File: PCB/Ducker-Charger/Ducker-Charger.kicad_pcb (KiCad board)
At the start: 4 copper layers, 61.8 x 130.1 mm, 194 parts, among them CN1 C_Pack04, IC1 STUSB4710AQ1TR, IC2 TPS54202HDDCT, IC3 BQ34Z100PWR-R2, J1 Conn_01x02, J2 Conn_01x05, J3 Conn_01x02, J4 USB_A, J5 USB_A, J6 Debug, J7 Conn_01x08, J8 Conn_01x07, Q1 BSC040N08NS5, Q10 AO3400A, Q11 AO3400A, Q12 BC846, Q15 BSC040N08NS5, Q16 BSC040N08NS5, Q17 BSC040N08NS5, Q18 BSC040N08NS5, Q19 BSC040N08NS5, Q2 BSC040N08NS5, Q6 AO4407A, Q7 AO3400A, Q8 AO4407A, Q9 AO3400A, SW1 EC11E15244G1, U1 BQ25713RSNR, U2 TPS25750DRJKR, U3 STPD01PUR, U4 TPS54302, U5 INA3221, U6 TPS54302, U7 STM32F401RBT6, U8 BQ7791500PWR, U9 ISO1540DR, Y1 16MHz

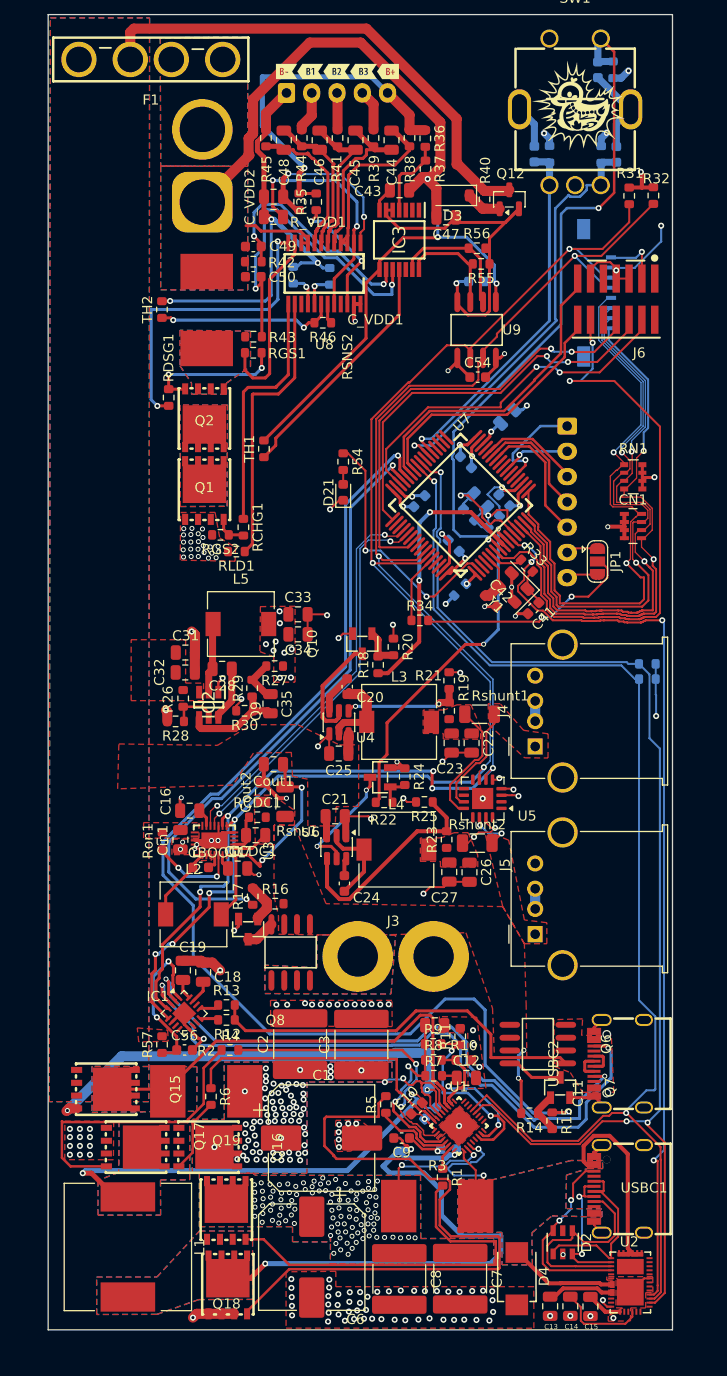
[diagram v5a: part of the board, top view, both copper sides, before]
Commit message: fix: removed 90deg tracks
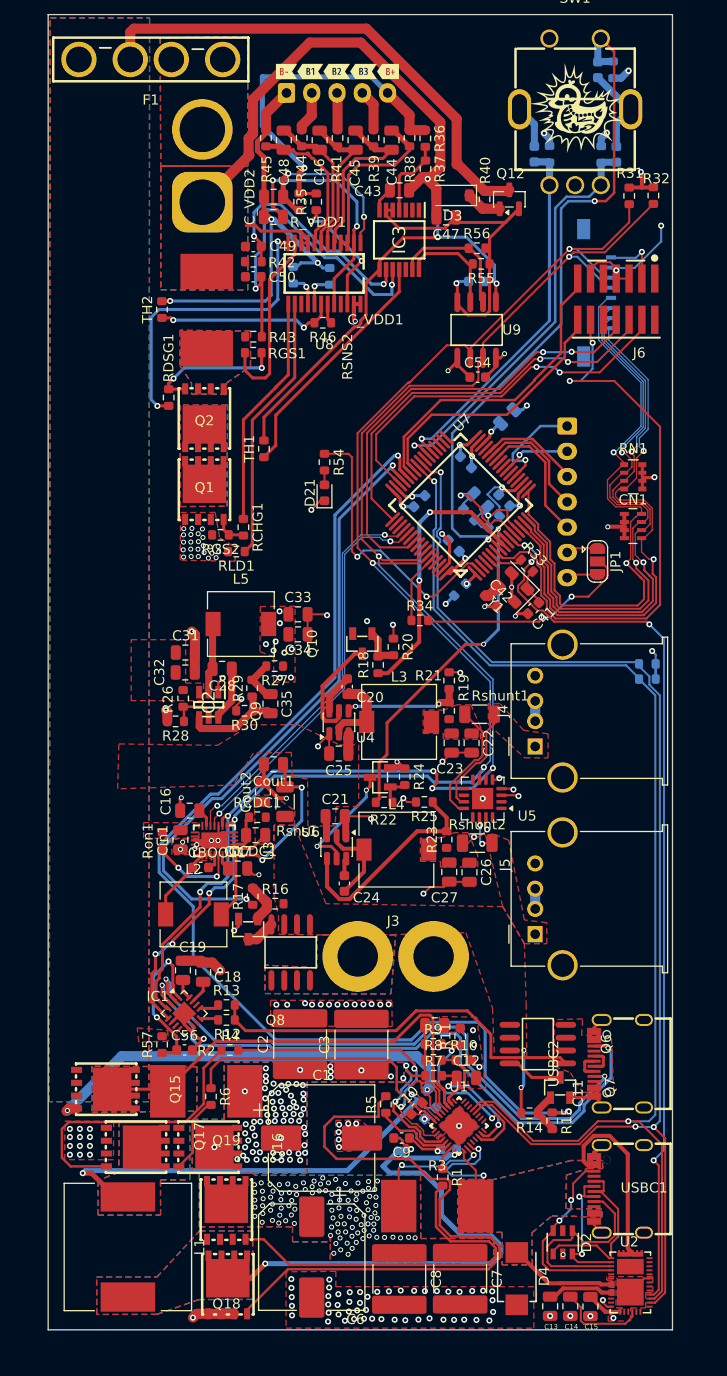
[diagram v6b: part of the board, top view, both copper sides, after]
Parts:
- moved G*** 2.20 mm to (197.8, 82.7)
- moved D21 1.85 mm to (194.7, 63.5)
- moved R54 1.85 mm to (194.7, 60.4)
- moved G*** 0.34 mm to (219.8, 25.3)
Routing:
- net /Logic/MCU_STATUS: track 25.5 -> 28.7 mm
- net /Logic/SWDIO: track 35.9 -> 37.9 mm
- net /High_pow/V_SYS_A: track 13.0 -> 11.2 mm
- net /BMS/I2C_LP.SCL: track 144.1 -> 145.8 mm
- net Net-(U8-CHG): track 24.7 -> 23.1 mm
- net /Logic/LAB_2ENABLER: track 115.0 -> 113.4 mm
- net GND: track 162.0 -> 160.4 mm
- net Net-(Q18-G): track 65.6 -> 64.1 mm
- net Net-(U8-LD): track 28.0 -> 26.5 mm
- net PD_IRQ: track 91.4 -> 90.1 mm
- net /Low_pow/5V_USB_A2: track 5.48 -> 4.25 mm
- net /High_pow/~{BATDRV}: track 46.4 -> 45.1 mm
- net /Logic/NTC_1: track 54.9 -> 56.0 mm
- net /Low_pow/IN-2: track 5.77 -> 4.90 mm
- net Net-(Q19-G): track 39.0 -> 38.1 mm
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
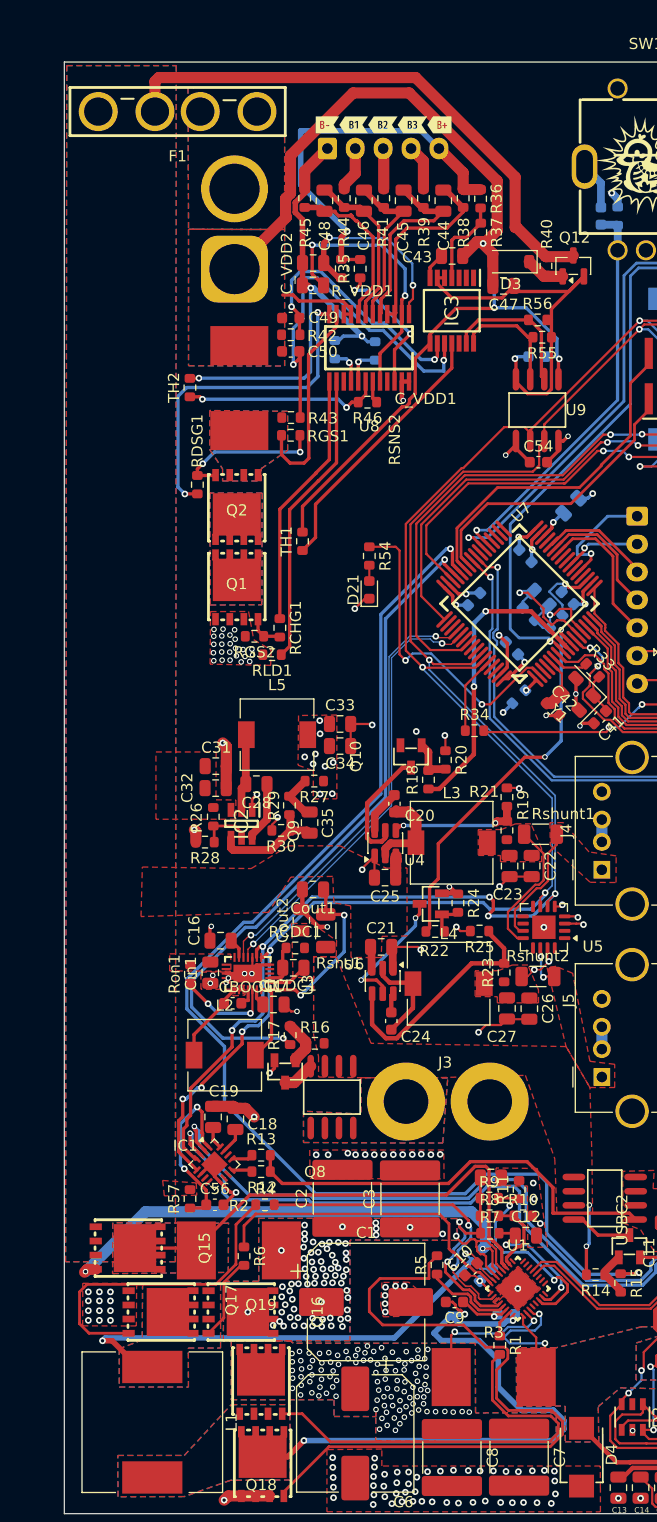
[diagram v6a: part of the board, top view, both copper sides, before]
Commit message: fix: downsized the numbers of load bearing VIAs
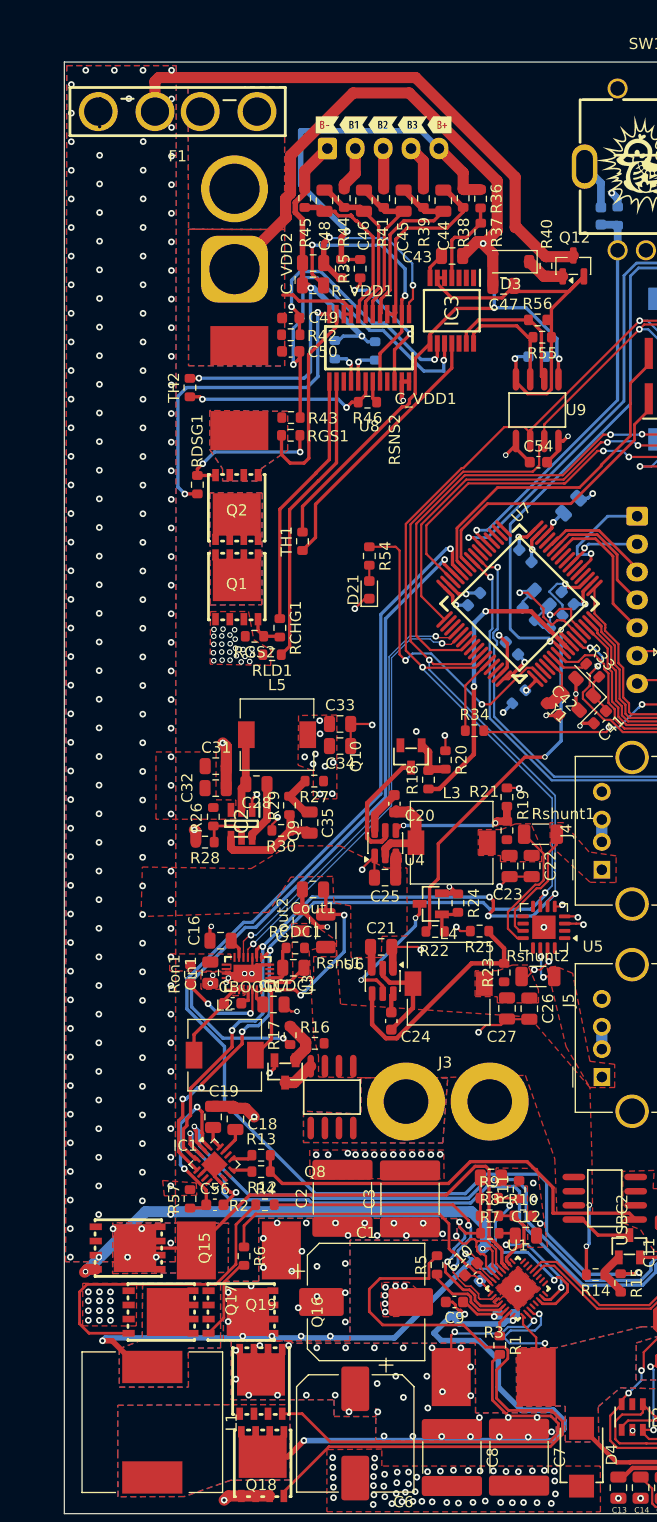
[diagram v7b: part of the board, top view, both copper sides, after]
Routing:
- net /High_pow/V_SYS_A: vias 73 -> 28
- net /High_pow/ACN: vias 108 -> 36
- net +BATT: vias 0 -> 172

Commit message: feat: remade the PCB & minor schematic fixes
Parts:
- removed C1, C6: 220u, Capacitor_SMD:CP_Elec_10x10
- removed C10, C20, C24, C29, C30, C36, C37, C40, C9: 100n, Capacitor_SMD:C_0603_1608Metric
- removed C11, C13, C14, C15: 4.7u, Capacitor_SMD:C_0805_2012Metric
- removed C12, C18, C19, C39: 1u, Capacitor_SMD:C_0805_2012Metric
- removed C16, C17: 4.7u 50V, Capacitor_SMD:C_0805_2012Metric
- removed C2, C3, C7, C8: 22u, Capacitor_SMD:C_2220_5750Metric
- removed C21, C25, C31: 10u, Capacitor_SMD:C_0805_2012Metric
- removed C22, C23, C26, C27, C33, C34: 22u, Capacitor_SMD:C_0805_2012Metric
- removed C28, C32: 0.1u, Capacitor_SMD:C_0805_2012Metric
- removed C35: 75p, Capacitor_SMD:C_0805_2012Metric
- removed C4, C5: 47n, Capacitor_SMD:C_0603_1608Metric
- removed C41, C42: 18p, Capacitor_SMD:C_0603_1608Metric
- removed C56: 1u, Capacitor_SMD:C_0603_1608Metric
- removed CBOOT1: 100n 50V, Capacitor_SMD:C_0603_1608Metric
- removed CCDC1: 4.7n, Capacitor_SMD:C_0805_2012Metric
- removed CN1: C_Pack04, Resistor_SMD:R_Array_Concave_4x0603
- removed CVBAT1: 100n, Resistor_SMD:R_0603_1608Metric
- removed Cin1: 10u 50V, Capacitor_SMD:C_0805_2012Metric
- removed Cout1, Cout2: 22u 25V, Capacitor_SMD:C_0805_2012Metric
- removed D2: USBLC6-4SC6, EasyEDA:SOT-23-6_L2.9-W1.6-P0.95-LS2.8-BL
- removed D21: LED, LED_SMD:LED_0603_1608Metric
- removed D4: SMBJ22A-E3/52, EasyEDA:SMB_L4.3-W3.6-LS5.4-RD
- removed FB1: FerriteBead, Inductor_SMD:L_0603_1608Metric
- removed IC1: STUSB4710AQ1TR, Package_DFN_QFN:QFN-16-1EP_3x3mm_P0.5mm_EP1.7x1.7mm
- removed IC2: TPS54202HDDCT, TPS54202HDDCT:SOT95P280X110-6N
- removed J3: Conn_01x02, TestPoint:TestPoint_Bridge_Pitch6.35mm_Drill1.3mm
- removed J8: Conn_01x07, Connector_JST:JST_XH_S7B-XH-A_1x07_P2.50mm_Horizontal
- removed JP1: Boot, Jumper:SolderJumper-3_P1.3mm_Open_RoundedPad1.0x1.5mm
- removed L1: 2.2u, Inductor_SMD:L_12x12mm_H6mm
- removed L2, L5: 10u, Inductor_SMD:L_6.3x6.3_H3
- removed L3, L4: 10u 5A, Inductor_SMD:L_7.3x7.3_H4.5
- removed Q10, Q11, Q7, Q9: AO3400A, EasyEDA:SOT-23-3_L2.9-W1.3-P1.90-LS2.4-BR
- removed Q15, Q16, Q17, Q18, Q19: BSC040N08NS5, EasyEDA:PG-TDSON-8_L5.9-W5.1-P1.27-LS6.2-BL
- removed Q6, Q8: AO4407A, EasyEDA:SOIC-8_L4.9-W3.9-P1.27-LS6.0-BL
- removed R1, R4, R5, R57, R6, R7: 10, Resistor_SMD:R_0603_1608Metric
- removed R10: 30k, Resistor_SMD:R_0603_1608Metric
- removed R11, R15, R17, R34, R9: 10k, Resistor_SMD:R_0603_1608Metric
- removed R12: 1k2, Resistor_SMD:R_0603_1608Metric
- removed R13: 50, Resistor_SMD:R_0603_1608Metric
- removed R14, R16, R19, R20, R23, R24, R27, Ron1: 100k, Resistor_SMD:R_0603_1608Metric
- removed R18, R22, R33, R54: 1k, Resistor_SMD:R_0603_1608Metric
- removed R2, R3: 5m, EasyEDA:R3920
- removed R21, R25: 13.3k, Resistor_SMD:R_0603_1608Metric
- removed R26: 511k, Resistor_SMD:R_0603_1608Metric
- removed R28: 105k, Resistor_SMD:R_0603_1608Metric
- removed R29: 22.1k, Resistor_SMD:R_0603_1608Metric
- removed R30: 0, Resistor_SMD:R_0603_1608Metric
- removed R8: 20k, Resistor_SMD:R_0603_1608Metric
- removed RCDC1: 5.6k, Resistor_SMD:R_0603_1608Metric
- removed RN1: R_Pack04, Resistor_SMD:R_Array_Convex_4x0603
- removed Rshunt1, Rshunt2, Rsns1: 10m, Resistor_SMD:R_1206_3216Metric
- removed U1: BQ25713RSNR, EasyEDA:QFN-32_L4.0-W4.0-P0.40-TL-EP2.8
- removed U2: TPS25750DRJKR, EasyEDA:QFN-38_L6.0-W4.0-P0.40-TL-EP_RJK
- removed U3: STPD01PUR, EasyEDA:QFN-24_L4.0-W3.0-P0.40-TL-EP
- removed U4, U6: TPS54302, Package_TO_SOT_SMD:SOT-23-6
- removed U5: INA3221, Package_DFN_QFN:Texas_RGV0016A_VQFN-16-1EP_4x4mm_P0.65mm_EP2.1x2.1mm
- removed U7: STM32F401RBT6, EasyEDA:LQFP-64_L10.0-W10.0-P0.50-LS12.0-BL
- removed Y1: 16MHz, Crystal:Crystal_SMD_EuroQuartz_MT-4Pin_3.2x2.5mm
- added C201: 1u, Capacitor_SMD:C_0805_2012Metric, B.Cu at (95.9, 172.6)
- added C202: 1u, Capacitor_SMD:C_0805_2012Metric, F.Cu at (124.6, 169.9)
- added C203: 10u 35V, Capacitor_SMD:C_1206_3216Metric, F.Cu at (123.4, 166.5)
- added C204: 10u 35V, Capacitor_SMD:C_1206_3216Metric, F.Cu at (121.1, 166.5)
- added C205: 3.3u, Capacitor_SMD:C_0805_2012Metric, F.Cu at (88.9, 173.0)
- added C206: 10u 35V, Capacitor_SMD:C_1206_3216Metric, F.Cu at (118.8, 166.5)
- added C207: 10u 16V, Capacitor_SMD:C_0603_1608Metric, F.Cu at (120.9, 150.7)
- added C208: 10u 35V, Capacitor_SMD:C_1206_3216Metric, F.Cu at (116.5, 166.5)
- added C209: 10u 35V, Capacitor_SMD:C_1206_3216Metric, F.Cu at (114.2, 166.5)
- added C210: 10u 35V, Capacitor_SMD:C_1206_3216Metric, F.Cu at (111.9, 166.5)
- added C211: 470n, Capacitor_SMD:C_0805_2012Metric, F.Cu at (110.9, 169.8)
- added C212: 10u 35V, Capacitor_SMD:C_1206_3216Metric, F.Cu at (117.1, 159.8)
- added C213: 22u 35V, Capacitor_SMD:C_1210_3225Metric, B.Cu at (117.1, 159.8)
- added C214: 33p, Capacitor_SMD:C_0603_1608Metric, F.Cu at (93.9, 161.5)
- added C215: 33n, Capacitor_SMD:C_0603_1608Metric, F.Cu at (99.9, 167.3)
- added C216: 22u 35V, Capacitor_SMD:C_1210_3225Metric, B.Cu at (117.1, 156.6)
- added C217: 1800p, Capacitor_SMD:C_0603_1608Metric, F.Cu at (92.4, 159.5)
- added C218: 680p, Capacitor_SMD:C_0603_1608Metric, F.Cu at (89.4, 159.0)
- added C219: 4.7u, Capacitor_SMD:C_0805_2012Metric, B.Cu at (131.6, 153.8)
- added C220: 100u 16V, Capacitor_SMD:C_1210_3225Metric, F.Cu at (116.9, 149.7)
- added C221: 15p, Capacitor_SMD:C_0603_1608Metric, F.Cu at (90.9, 161.0)
- added C222: 10n, Capacitor_SMD:C_0603_1608Metric, F.Cu at (106.5, 174.9)
- added C223: 100u 16V, Capacitor_SMD:C_1210_3225Metric, F.Cu at (113.6, 149.7)
- added C224: 100p, Capacitor_SMD:C_0603_1608Metric, B.Cu at (97.5, 165.0)
- added C225: 100u 16V, Capacitor_SMD:C_1210_3225Metric, F.Cu at (110.4, 149.7)
- added C226: 10u 16V, Capacitor_SMD:C_0603_1608Metric, F.Cu at (119.4, 150.7)
- added C227: 100p, Capacitor_SMD:C_0603_1608Metric, B.Cu at (93.8, 162.3)
- added C228: 10u, Capacitor_SMD:C_0805_2012Metric, F.Cu at (105.9, 155.7)
- added C229: 47n, Capacitor_SMD:C_0603_1608Metric, F.Cu at (92.7, 172.5)
- added C230: 10u, Capacitor_SMD:C_0805_2012Metric, F.Cu at (105.8, 153.7)
- added C231: 47n, Capacitor_SMD:C_0603_1608Metric, F.Cu at (74.9, 177.6)
- added C232: 10u 25V, Capacitor_SMD:C_1206_3216Metric, F.Cu at (92.9, 87.9)
- added C233: 330p, Capacitor_SMD:C_0603_1608Metric, B.Cu at (115.1, 149.9)
- added C234: 330p, Capacitor_SMD:C_0603_1608Metric, B.Cu at (115.2, 148.4)
- added C235: 10u 25V, Capacitor_SMD:C_1206_3216Metric, F.Cu at (73.4, 166.3)
- added C236: 10u 25V, Capacitor_SMD:C_1206_3216Metric, F.Cu at (73.4, 164.0)
- added C237: 10u 25V, Capacitor_SMD:C_1206_3216Metric, F.Cu at (73.4, 175.7)
- added C238: 10u 25V, Capacitor_SMD:C_1206_3216Metric, F.Cu at (73.4, 173.3)
- added C239: 10u 25V, Capacitor_SMD:C_1206_3216Metric, F.Cu at (73.4, 171.0)
- added C240: 10u 25V, Capacitor_SMD:C_1206_3216Metric, F.Cu at (73.4, 168.7)
- added C241: 1u, Capacitor_SMD:C_0805_2012Metric, F.Cu at (82.3, 159.5)
- added C242: 100n, Capacitor_SMD:C_0603_1608Metric, F.Cu at (99.9, 84.9)
- added C243: 0.1, Capacitor_SMD:C_0805_2012Metric, F.Cu at (74.7, 152.4)
- added C244: 22u 16V, Capacitor_SMD:C_0805_2012Metric, F.Cu at (94.9, 81.4)
- added C245: 22u 16V, Capacitor_SMD:C_0805_2012Metric, F.Cu at (92.4, 81.4)
- added C246: 100n, Capacitor_SMD:C_0603_1608Metric, F.Cu at (108.0, 150.5)
- added C301: 4.7u 50V, Capacitor_SMD:C_0805_2012Metric, F.Cu at (86.3, 137.7)
- added C302: 4.7u 50V, Capacitor_SMD:C_0805_2012Metric, B.Cu at (96.8, 135.4)
- added C303: 10u 25V, Capacitor_SMD:C_1206_3216Metric, F.Cu at (93.0, 100.6)
- added C304: 10u 25V, Capacitor_SMD:C_1206_3216Metric, F.Cu at (93.0, 122.8)
- added C305: 1u, Capacitor_SMD:C_0805_2012Metric, F.Cu at (118.3, 139.0)
- added C306: 100n, Capacitor_SMD:C_0603_1608Metric, F.Cu at (100.0, 97.6)
- added C307: 100n, Capacitor_SMD:C_0603_1608Metric, F.Cu at (100.0, 119.8)
- added C308: 1u, Capacitor_SMD:C_0603_1608Metric, F.Cu at (122.9, 138.0)
- added C309: 1u, Capacitor_SMD:C_0805_2012Metric, F.Cu at (120.3, 139.0)
- added C310: 22u, Capacitor_SMD:C_0805_2012Metric, F.Cu at (92.5, 94.1)
- added C311: 22u, Capacitor_SMD:C_0805_2012Metric, F.Cu at (95.0, 116.3)
- added C312: 22u, Capacitor_SMD:C_0805_2012Metric, F.Cu at (95.0, 94.1)
- added C313: 22u, Capacitor_SMD:C_0805_2012Metric, F.Cu at (92.5, 116.3)
- added C401: 100n, Capacitor_SMD:C_0603_1608Metric, B.Cu at (119.6, 64.2)
- added C402: 100n, Capacitor_SMD:C_0603_1608Metric, B.Cu at (117.9, 76.4)
- added C404: 1u, Capacitor_SMD:C_0805_2012Metric, F.Cu at (130.6, 78.7)
- added C405: 100n, Capacitor_SMD:C_0603_1608Metric, F.Cu at (128.6, 78.7)
- added C406: 100n, Capacitor_SMD:C_0603_1608Metric, B.Cu at (124.6, 68.4)
- added C407: 100n, Capacitor_SMD:C_0603_1608Metric, B.Cu at (106.9, 68.9)
- added C409: 18p, Capacitor_SMD:C_0603_1608Metric, F.Cu at (126.1, 82.4)
- added C412: 18p, Capacitor_SMD:C_0603_1608Metric, F.Cu at (121.1, 81.2)
- added C413: 10u 25V, Capacitor_SMD:C_1206_3216Metric, F.Cu at (92.7, 111.7)
- added C414: 0.1u, Capacitor_SMD:C_0805_2012Metric, F.Cu at (95.2, 111.7)
- added C415: 100n, Capacitor_SMD:C_0603_1608Metric, B.Cu at (130.1, 45.6)
- added C416: 100n, Capacitor_SMD:C_0805_2012Metric, F.Cu at (100.2, 108.7)
- added C417: 22u, Capacitor_SMD:C_0805_2012Metric, F.Cu at (95.2, 105.3)
- added C418: 22u, Capacitor_SMD:C_0805_2012Metric, F.Cu at (92.7, 105.3)
- added C419: 75p, Capacitor_SMD:C_0805_2012Metric, F.Cu at (107.7, 111.7)
- added C420: 100n, Capacitor_SMD:C_0603_1608Metric, F.Cu at (129.2, 65.2)
- added CBOOT301: 100n 50V, Capacitor_SMD:C_0603_1608Metric, F.Cu at (96.8, 136.5)
- added CCDC301: 4.7n, Capacitor_SMD:C_0805_2012Metric, F.Cu at (93.6, 131.1)
- added CN401: 100n, Resistor_SMD:R_Array_Concave_4x0603, F.Cu at (130.2, 69.5)
- added CVBAT401: 100n, Resistor_SMD:R_0603_1608Metric, B.Cu at (111.9, 81.9)
- added Cin301: 10u 50V, Capacitor_SMD:C_0805_2012Metric, F.Cu at (87.0, 141.7)
- added Cout301: 22u 35V, Capacitor_SMD:C_1210_3225Metric, F.Cu at (105.7, 142.0)
- added Cout302: 22u 35V, Capacitor_SMD:C_1210_3225Metric, F.Cu at (111.0, 142.1)
- added D201: USBLC6-4SC6, EasyEDA:SOT-23-6_L2.9-W1.6-P0.95-LS2.8-BL, B.Cu at (123.2, 155.5)
- added D202: LED, LED_SMD:LED_0603_1608Metric, F.Cu at (106.0, 159.7)
- added D301: USBLC6-4SC6, EasyEDA:SOT-23-6_L2.9-W1.6-P0.95-LS2.8-BL, B.Cu at (123.3, 135.7)
- added D401: LED, LED_SMD:LED_0603_1608Metric, F.Cu at (120.2, 85.2)
- added FB401: FerriteBead, Inductor_SMD:L_0603_1608Metric, F.Cu at (126.9, 78.7)
- added G***: LOGO, LOGO, F.Cu at (176.7, 110.9)
- added IC301: STUSB4710AQ1TR, Package_DFN_QFN:QFN-16-1EP_3x3mm_P0.5mm_EP1.7x1.7mm, F.Cu at (118.8, 135.1)
- added IC401: TPS54202HDDCT, TPS54202HDDCT:SOT95P280X110-6N, F.Cu at (98.5, 111.7)
- added J303: Conn_01x02, TerminalBlock:TerminalBlock_bornier-2_P5.08mm, B.Cu at (125.1, 125.8)
- added J404: Conn_01x08, Connector_JST:JST_EH_B8B-EH-A_1x08_P2.50mm_Vertical, F.Cu at (97.4, 67.2)
- added JP401: Boot, Jumper:SolderJumper-3_P1.3mm_Open_RoundedPad1.0x1.5mm, F.Cu at (107.1, 81.2)
- added JP402: BL_NODE, Jumper:SolderJumper-3_P1.3mm_Open_RoundedPad1.0x1.5mm, B.Cu at (119.6, 55.4)
- added L201: 2.2u 20A, Inductor_SMD:L_Chilisin_BMRF00131360, F.Cu at (90.6, 180.8)
- added L202: 10u 5A, Inductor_SMD:L_7.3x7.3_H4.5, F.Cu at (87.4, 85.4)
- added L301: 10u 5A, Inductor_SMD:L_7.3x7.3_H4.5, F.Cu at (98.5, 141.2)
- added L302: 10u 5A, Inductor_SMD:L_7.3x7.3_H4.5, F.Cu at (87.5, 98.1)
- added L303: 10u 5A, Inductor_SMD:L_7.3x7.3_H4.5, F.Cu at (87.5, 120.3)
- added L401: 10u, Inductor_SMD:L_6.3x6.3_H3, F.Cu at (87.7, 109.2)
- added NT401: NetTie_2, NetTie:NetTie-2_SMD_Pad0.5mm, F.Cu at (128.6, 80.2)
- added Q201: BSC040N08NS5, EasyEDA:PG-TDSON-8_L5.9-W5.1-P1.27-LS6.2-BL, F.Cu at (100.1, 173.9)
- added Q202: BSC040N08NS5, EasyEDA:PG-TDSON-8_L5.9-W5.1-P1.27-LS6.2-BL, F.Cu at (101.9, 180.9)
- added Q203: BSC040N08NS5, EasyEDA:PG-TDSON-8_L5.9-W5.1-P1.27-LS6.2-BL, F.Cu at (78.1, 180.8)
- added Q204: BSC040N08NS5, EasyEDA:PG-TDSON-8_L5.9-W5.1-P1.27-LS6.2-BL, F.Cu at (79.3, 174.4)
- added Q205: AO4407A, EasyEDA:SOIC-8_L4.9-W3.9-P1.27-LS6.0-BL, F.Cu at (79.4, 164.4)
- added Q301: AO3400A, EasyEDA:SOT-23-3_L2.9-W1.3-P1.90-LS2.4-BR, B.Cu at (103.5, 98.0)
- added Q302: AO3400A, EasyEDA:SOT-23-3_L2.9-W1.3-P1.90-LS2.4-BR, B.Cu at (103.5, 120.2)
- added Q303: AO3400A, EasyEDA:SOT-23-3_L2.9-W1.3-P1.90-LS2.4-BR, B.Cu at (105.6, 138.3)
- added Q304: AO3400A, EasyEDA:SOT-23-3_L2.9-W1.3-P1.90-LS2.4-BR, B.Cu at (105.7, 130.8)
- added Q305: AO4407A, EasyEDA:SOIC-8_L4.9-W3.9-P1.27-LS6.0-BL, B.Cu at (111.6, 140.2)
- added Q306: AO4407A, EasyEDA:SOIC-8_L4.9-W3.9-P1.27-LS6.0-BL, B.Cu at (111.7, 132.7)
- added Q401: AO3400A, EasyEDA:SOT-23-3_L2.9-W1.3-P1.90-LS2.4-BR, B.Cu at (113.6, 54.0)
- added Q402: PMOS, EasyEDA:SOT-23-3_L2.9-W1.3-P1.90-LS2.4-BR, B.Cu at (113.9, 57.6)
- added R201: 10, Resistor_SMD:R_0603_1608Metric, B.Cu at (95.8, 170.9)
- added R202: 10k, Resistor_SMD:R_0603_1608Metric, B.Cu at (111.6, 159.6)
- added R203: 383k, Resistor_SMD:R_0603_1608Metric, F.Cu at (97.4, 166.5)
- added R204: 220k, Resistor_SMD:R_0603_1608Metric, F.Cu at (97.4, 168.0)
- added R205: 2.2, Resistor_SMD:R_0603_1608Metric, F.Cu at (125.3, 165.7)
- added R206: 10k, Resistor_SMD:R_0603_1608Metric, B.Cu at (111.6, 161.1)
- added R207: 330k, Resistor_SMD:R_0603_1608Metric, F.Cu at (87.9, 162.5)
- added R208: 1M, Resistor_SMD:R_0603_1608Metric, F.Cu at (86.4, 162.0)
- added R209: 1, Resistor_SMD:R_0603_1608Metric, F.Cu at (110.0, 165.7)
- added R210: 4.99, Resistor_SMD:R_0603_1608Metric, F.Cu at (102.2, 166.5)
- added R211: 40.2k, Resistor_SMD:R_0603_1608Metric, F.Cu at (92.4, 162.5)
- added R212: 10m, EasyEDA:R3920, F.Cu at (106.5, 167.3)
- added R213: 10k, Resistor_SMD:R_0603_1608Metric, F.Cu at (89.4, 162.5)
- added R214: 4.99, Resistor_SMD:R_0603_1608Metric, F.Cu at (102.2, 168.0)
- added R215: 137k, Resistor_SMD:R_0603_1608Metric, B.Cu at (97.5, 163.5)
- added R216: 10k, Resistor_SMD:R_0603_1608Metric, B.Cu at (96.3, 169.4)
- added R217: 30k, Resistor_SMD:R_0603_1608Metric, B.Cu at (92.1, 161.6)
- added R218: 150k, Resistor_SMD:R_0603_1608Metric, B.Cu at (100.9, 85.3)
- added R219: 27k, Resistor_SMD:R_0603_1608Metric, B.Cu at (100.9, 88.7)
- added R220: 10, Resistor_SMD:R_0603_1608Metric, F.Cu at (71.9, 153.6)
- added R221: 10m, EasyEDA:R3920, F.Cu at (79.5, 152.6)
- added R222: 10, Resistor_SMD:R_0603_1608Metric, F.Cu at (71.9, 151.1)
- added R223: 1k, Resistor_SMD:R_0603_1608Metric, F.Cu at (106.1, 157.7)
- added R224: 100k, Resistor_SMD:R_0603_1608Metric, F.Cu at (104.5, 87.9)
- added R225: 13.3k, Resistor_SMD:R_0603_1608Metric, F.Cu at (102.4, 87.9)
- added R301: 1k, Resistor_SMD:R_0603_1608Metric, B.Cu at (103.0, 94.5)
- added R302: 1k, Resistor_SMD:R_0603_1608Metric, B.Cu at (103.0, 116.7)
- added R303: 100k, Resistor_SMD:R_0603_1608Metric, B.Cu at (105.5, 95.5)
- added R304: 100k, Resistor_SMD:R_0603_1608Metric, B.Cu at (105.5, 117.7)
- added R305: 10k, Resistor_SMD:R_0603_1608Metric, B.Cu at (104.2, 142.7)
- added R306: 10k, Resistor_SMD:R_0603_1608Metric, B.Cu at (104.3, 134.9)
- added R307: 100k, Resistor_SMD:R_0603_1608Metric, B.Cu at (106.6, 141.9)
- added R308: 100k, Resistor_SMD:R_0603_1608Metric, B.Cu at (106.7, 134.4)
- added R309: 10k, Resistor_SMD:R_0603_1608Metric, B.Cu at (101.0, 98.1)
- added R310: 10k, Resistor_SMD:R_0603_1608Metric, B.Cu at (101.0, 120.3)
- added R311: 10, Resistor_SMD:R_0603_1608Metric, F.Cu at (122.1, 140.3)
- added R312: 100k, Resistor_SMD:R_0603_1608Metric, F.Cu at (104.5, 100.6)
- added R313: 13.3k, Resistor_SMD:R_0603_1608Metric, F.Cu at (102.5, 100.6)
- added R314: 100k, Resistor_SMD:R_0603_1608Metric, F.Cu at (104.5, 122.8)
- added R315: 13.3k, Resistor_SMD:R_0603_1608Metric, F.Cu at (102.5, 122.8)
- added R316: 1k2, Resistor_SMD:R_0603_1608Metric, F.Cu at (123.8, 133.8)
- added R317: 50, Resistor_SMD:R_0603_1608Metric, F.Cu at (125.0, 139.5)
- added R402: 220, Resistor_SMD:R_0603_1608Metric, F.Cu at (123.6, 78.9)
- added R405: 511k, Resistor_SMD:R_0603_1608Metric, B.Cu at (102.4, 112.0)
- added R406: 105k, Resistor_SMD:R_0603_1608Metric, B.Cu at (100.2, 112.0)
- added R407: 10k, Resistor_SMD:R_0603_1608Metric, F.Cu at (109.9, 80.2)
- added R408: 1k, Resistor_SMD:R_0603_1608Metric, F.Cu at (119.1, 82.3)
- added R413: 22.1k, Resistor_SMD:R_0603_1608Metric, F.Cu at (105.7, 111.7)
- added R414: 4k87, Resistor_SMD:R_0603_1608Metric, F.Cu at (103.7, 111.7)
- added R415: 10k, Resistor_SMD:R_0603_1608Metric, F.Cu at (127.6, 66.9)
- added R416: 1k, Resistor_SMD:R_0603_1608Metric, B.Cu at (117.6, 54.1)
- added R417: 10k, Resistor_SMD:R_0603_1608Metric, B.Cu at (116.1, 54.1)
- added R418: 1k, Resistor_SMD:R_0603_1608Metric, B.Cu at (117.6, 57.1)
- added R419: 10k, Resistor_SMD:R_0603_1608Metric, B.Cu at (116.1, 57.1)
- added R420: 4k7, Resistor_SMD:R_0603_1608Metric, B.Cu at (114.6, 65.8)
- added RCDC301: 10k, Resistor_SMD:R_0603_1608Metric, F.Cu at (91.1, 132.1)
- added RCDC302: 5.6k, Resistor_SMD:R_0603_1608Metric, F.Cu at (93.4, 132.9)
- added RN401: 10k, Resistor_SMD:R_Array_Convex_4x0603, F.Cu at (130.4, 74.4)
- added Ron301: 100k, Resistor_SMD:R_0603_1608Metric, B.Cu at (96.6, 137.2)
- added Rshunt301: 10m, Resistor_SMD:R_1206_3216Metric, F.Cu at (113.6, 94.9)
- added Rshunt302: 10m, Resistor_SMD:R_1206_3216Metric, F.Cu at (113.7, 112.9)
- added Rsns301: 25m, Resistor_SMD:R_1206_3216Metric, F.Cu at (108.1, 138.3)
- added SW403: Reset, Button_Switch_SMD:SW_SPST_FSMSM, B.Cu at (132.9, 43.0)
- added TH401: Thermistor_NTC, Resistor_SMD:R_0603_1608Metric, F.Cu at (126.4, 64.2)
- added U201: BQ25713RSNR, EasyEDA:QFN-32_L4.0-W4.0-P0.40-TL-EP2.8, F.Cu at (90.9, 167.5)
- added U202: TPS25750DRJKR, EasyEDA:QFN-38_L6.0-W4.0-P0.40-TL-EP_RJK, F.Cu at (111.2, 155.0)
- added U203: TPS54302, Package_TO_SOT_SMD:SOT-23-6, F.Cu at (98.1, 87.9)
- added U301: INA3221, Package_DFN_QFN:Texas_RGV0016A_VQFN-16-1EP_4x4mm_P0.65mm_EP2.1x2.1mm, B.Cu at (113.2, 103.9)
- added U302: STPD01PUR, EasyEDA:QFN-24_L4.0-W3.0-P0.40-TL-EP, F.Cu at (91.2, 136.9)
- added U303: TPS54302, Package_TO_SOT_SMD:SOT-23-6, F.Cu at (98.3, 100.6)
- added U304: TPS54302, Package_TO_SOT_SMD:SOT-23-6, F.Cu at (98.3, 122.8)
- added U401: STM32F401RBT6, EasyEDA:LQFP-64_L10.0-W10.0-P0.50-LS12.0-BL, F.Cu at (115.9, 72.9)
- added Y401: 16MHz, Crystal:Crystal_SMD_EuroQuartz_MT-4Pin_3.2x2.5mm, F.Cu at (123.6, 81.9)
- D501: renamed from D3; value D_Zener -> 5V
- R515: renamed from R40; value 220k -> 15k
- RDSG501: renamed from RDSG1; value 4k5 -> 1k
- moved R410 122.4 mm to (131.0, 156.7), turned to -90 degrees
- moved R412 120.3 mm to (132.5, 156.7), turned to -90 degrees
- moved R411 106.0 mm to (120.2, 51.4)
- moved R409 106.0 mm to (122.6, 51.3)
- moved USBC201 96.7 mm to (130.1, 155.9)
- moved USBC301 95.3 mm to (130.0, 136.2)
- moved TH502 94.9 mm to (94.6, 71.2)
- moved J301 94.3 mm to (121.7, 97.8)
- moved C403 94.3 mm to (127.9, 30.5)
- moved C410 94.3 mm to (121.6, 38.9)
- moved C501 94.3 mm to (107.5, 37.5)
- moved C502 94.3 mm to (103.9, 37.5)
- moved C504 94.3 mm to (96.8, 37.5)
- moved F101 94.3 mm to (83.7, 29.5)
- moved IC501 94.3 mm to (108.2, 47.3)
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- renumbered C53 to C403, C38 to C408, C51 to C410, C52 to C411, C44 to C501, C45 to C502, C46 to C503, C48 to C504, C49 to C505, C50 to C506, C55 to C507, C54 to C508, C43 to C509, C47 to C510, C_VDD1 to C_VDD501, C_VDD2 to C_VDD502, F1 to F101, IC3 to IC501, J1 to J101, J2 to J102, J4 to J301, J5 to J302, J6 to J401, J7 to J403, Q1 to Q501, Q2 to Q502, Q12 to Q503, R51 to R401, R49 to R403, R50 to R404, R32 to R409, R53 to R410, R31 to R411, R52 to R412, R47 to R501, R38 to R502, R39 to R503, R41 to R504, R44 to R505, R45 to R506, R48 to R507, R42 to R508, R43 to R509, R46 to R510, R35 to R511, R36 to R512, R37 to R513, R56 to R514, R55 to R516, RCHG1 to RCHG501, RGS1 to RGS501, RGS2 to RGS502, RLD1 to RLD501, RSNS2 to RSNS501, R_VDD1 to R_VDD501, SW1 to SW401, TH2 to TH501, TH1 to TH502, U8 to U501, U9 to U502, USBC1 to USBC201, USBC2 to USBC301
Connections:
- net /High_pow/ACP renamed /High_pow/V_WIRE
- net /High_pow/DN renamed /High_pow/D-
- net /High_pow/DP renamed /High_pow/D+
- J403 pad 1: /Logic/NTC_1 -> /Logic/NTC_4
- J403 pad 2: /Logic/NTC_2 -> /Logic/NTC_3
- J403 pad 3: /Logic/NTC_3 -> /Logic/NTC_2
- J403 pad 4: /Logic/NTC_4 -> /Logic/NTC_1
- J403 pad 7: GND -> GNDA
- J403 pad 8: +3V3 -> +3.3VA
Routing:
- net VSYS: track 0.00 -> 228.1 mm, vias 0 -> 8
- net /High_pow/HP.CHRG_OK: track 0.00 -> 165.9 mm, vias 0 -> 4
- net /High_pow/HP.EN_OTG: track 0.00 -> 160.1 mm, vias 0 -> 4
- net /High_pow/HP.IADPT: track 0.00 -> 156.6 mm, vias 0 -> 3
- net /High_pow/HP.PSYS: track 0.00 -> 154.8 mm, vias 0 -> 3
- net /High_pow/HP.IBAT: track 0.00 -> 152.3 mm, vias 0 -> 3
- net /High_pow/HP.PD_IRQ: track 0.00 -> 140.7 mm, vias 0 -> 3
- net /Logic/C2.ST_EN: track 0.00 -> 129.3 mm, vias 0 -> 4
- net /Logic/C2.ST_INT: track 0.00 -> 126.5 mm, vias 0 -> 4
- net +5V: track 0.00 -> 114.3 mm, vias 0 -> 5
- net /Logic/LAB_2ENABLER: track 113.4 -> 0.00 mm, vias 2 -> 0
- net /Logic/C2.RDY: track 0.00 -> 96.2 mm, vias 0 -> 3
- net PD_IRQ: track 90.1 -> 0.00 mm, vias 4 -> 0
- net /BMS/I2C_LP.SCL: track 145.8 -> 233.8 mm, vias 7 -> 6
- net /BMS/I2C_LP.SDA: track 143.5 -> 223.6 mm, vias 7 -> 8
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- added copper zone on F.Cu, net +5V
- added copper zone on F.Cu, net /High_pow/2USB
- added copper zone on B.Cu, net /Low_pow/VBUS
- added copper zone on B.Cu, net /Low_pow/V_OUT_AUX
- added copper zone on F.Cu, net Net-(C222-Pad1)
- added copper zone on F.Cu, net Net-(C241-Pad1)
- added copper zone on F.Cu, net Net-(CBOOT301-Pad2)
- added copper zone on B.Cu, net Net-(IC401-SW)
- added copper zone on F.Cu, net Net-(IC401-SW)
- added copper zone on B.Cu, net Net-(U203-SW)
- added copper zone on F.Cu, net Net-(U203-SW)
- added copper zone on F.Cu, net Net-(U302-ISNS+)
- added copper zone on F.Cu, net Net-(U302-VSNS)
- added copper zone on B.Cu, net Net-(U303-SW)
- added copper zone on F.Cu, net Net-(U303-SW)
- added copper zone on B.Cu, net Net-(U304-SW)
- added copper zone on F.Cu, net Net-(U304-SW)
- added copper zone on F.Cu, net VSYS
- removed copper zone on B.Cu, net /High_pow/ACN
- removed copper zone on F.Cu, net /High_pow/ACN
- removed copper zone on In1.Cu, net /High_pow/ACN
- removed copper zone on In2.Cu, net /High_pow/ACN
- removed copper zone on B.Cu, net /High_pow/SW1
- removed copper zone on In1.Cu, net /High_pow/SW1
- removed copper zone on In2.Cu, net /High_pow/SW1
- removed copper zone on B.Cu, net /High_pow/SW2
- removed copper zone on In1.Cu, net /High_pow/SW2
- removed copper zone on In2.Cu, net /High_pow/SW2
- removed copper zone on B.Cu, net /High_pow/V_SYS_A
- removed copper zone on F.Cu, net /High_pow/V_SYS_A
- removed copper zone on In1.Cu, net /High_pow/V_SYS_A
- removed copper zone on In2.Cu, net /High_pow/V_SYS_A
- removed copper zone on B.Cu, net /High_pow/V_SYS_B
- removed copper zone on F.Cu, net /High_pow/V_SYS_B
- removed copper zone on In1.Cu, net /High_pow/V_SYS_B
- removed copper zone on In2.Cu, net /High_pow/V_SYS_B
- removed copper zone on B.Cu, net /High_pow/V_WIRE
- removed copper zone on F.Cu, net /Low_pow/IN-1
- removed copper zone on F.Cu, net /Low_pow/IN-2
- removed copper zone on F.Cu, net /Low_pow/VBUS
- removed copper zone on F.Cu, net /Low_pow/V_LABS
- removed copper zone on In1.Cu, net /Low_pow/V_LABS
- removed copper zone on F.Cu, net Net-(CBOOT1-Pad2)
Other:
- board size 61.8 x 130.1 mm -> 66.4 x 163.6 mm
- board text added: "{ "ViaStitching": "0.2", "stitch_zone_0": { "HSpacing": "1", "VSpacing": "1", "HOffset": "0", "VOffset": "0", "Clearance": "0", "Randomize": false } }"
